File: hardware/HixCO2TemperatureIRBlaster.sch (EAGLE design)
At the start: 33 parts, among them J1 FTDI, J2 IEC320C8, J3 XH4P, Q1 AO3400, Q2 AO3400, U1 ESP12E, U2 LM3940, U3 HLK-PM01, U4 DS18B20

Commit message: update hardware
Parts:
- removed C3: 100nF, resistor:C-EUC1206
- removed R1, R3, R4: 10K, rcl:R-EU_R1206
- removed R13: 2.2K, rcl:R-EU_R1206
- removed S1: PROG, 0_HixField:PUSHBTN
- removed S2: RST, 0_HixField:PUSHBTN
- removed U1: ESP12E, 0_HixField:ESP8266(ESP12E)SMD
- added C5: 100nF, resistor:C-EUC1206
- added R10, R11, R15: 10K, rcl:R-EU_R1206
- added R12: 2.2K, rcl:R-EU_R1206
- added S3: RST, 0_HixField:PUSHBTNSMALL
- added S4: PROG, 0_HixField:PUSHBTNSMALL
- added U$1: MHZ-19_CO2, 0_HixField:MHZ-19_CO2
- added U$2: ESP8266(ESP12E)V2, 0_HixField:ESP8266(ESP12E)V2
- C1, C2: device resistor:C-EUC1206 -> rcl:CPOL-EUSMCA
- C6: device resistor:CPOL-EUE3.5-8 -> 0_HixField:ELCO
- IRLED1, IRLED2, IRLED3: value (none) -> LEDLED5MM_ANGLED1; device led:LED5MM -> 0_HixField:LEDLED5MM_ANGLED1
- R8, R9: device resistor:R-EU_R1206 -> rcl:R-EU_R1206
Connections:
- removed net ENABLE: R3.1, U1.ENABLE
- removed net GPIO0: R2.1, S1.1, U1.GPIO0
- removed net GPIO15: R4.2, U1.GPIO15
- removed net RESET: R1.1, S2.1, U1.RESET
- new net N$10: R2.2, U$2.CS_TXD2_GPIO15
- new net N$11: U$2.GPIO16_WAKE
- new net N$7: R10.1, S3.1, U$2.RST
- new net N$8: R11.1, U$2.ENABLE
- new net N$9: R15.1, S4.1, U$2.FLASH_GPIO0
- net 3.3V: now also C2.+, C5.1, J3.2, R10.2, R11.2, R12.2, R15.2, U$2.VCC; no longer C2.1, C3.1, R1.2, R13.2, R2.2, R3.2, U1.VCC
- net 5.0V: now also C1.+; no longer C1.1, J3.2
- net BEEP: now also R12.1, U$2.TXD1_GPIO2; no longer R13.1, U1.GPIO2
- net GND: now also C1.-, C2.-, C5.2, R2.1, S3.2, S4.2, U$2.GND; no longer C1.2, C2.2, C3.2, R4.1, S1.2, S2.2, U1.GND
- net IR_IN: now also U$2.GPIO14_SCLK; no longer U1.GPIO14
- net IR_OUT: now also U$2.GPIO13_MOSI; no longer U1.GPIO13
- net RXD: now also U$2.TXD0_GPIO1; no longer U1.TX
- net SCL: now also U$2.SCL_GPIO5; no longer U1.GPIO5
- net SDA: now also U$2.SDA_GPIO4; no longer U1.GPIO4
- net TEMP: now also U$2.GPIO12_MISO; no longer U1.GPIO12
- net TXD: now also U$2.RXD0_GPIO3; no longer U1.RX

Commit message: continued working on hardware models
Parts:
- C4: device resistor:C-EUC1206 -> rcl:C-EUC1206
- C5: device resistor:C-EUC1206 -> rcl:C-EUC1206; SPICEPREFIX (none) -> C
- C6: device 0_HixField:ELCO -> 0_HixField:ELCOELKO_RADIAL_STRAIGHT_4P_8D_9H
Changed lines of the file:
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@@
 <part name="F1" library="0_HixField" deviceset="FUSE" device="" value="800mA"/>
 <part name="R14" library="0_HixField" library_urn="urn:adsk.eagle:library:13392178" deviceset="S10K275" device="" package3d_urn="urn:adsk.eagle:package:12836052/2" value="S10K275"/>
-<part name="C6" library="0_HixField" library_urn="urn:adsk.eagle:library:13392178" deviceset="ELCO" device="" package3d_urn="urn:adsk.eagle:package:13392182/1" value="680μF/6.3V"/>
+<part name="C6" library="0_HixField" library_urn="urn:adsk.eagle:library:13392178" deviceset="ELCO" device="ELKO_RADIAL_STRAIGHT_4P_8D_9H" package3d_urn="urn:adsk.eagle:package:17790431/3" value="680μF/6.3V"/>
 <part name="SUPPLY1" library="0_HixField" library_urn="urn:adsk.eagle:library:13392178" deviceset="5.0V" device=""/>
 <part name="SUPPLY2" library="0_HixField" library_urn="urn:adsk.eagle:library:13392178" deviceset="3.3V" device=""/>
 <part name="J2" library="0_HixField" library_urn="urn:adsk.eagle:library:13392178" deviceset="IEC320C8" device="" package3d_urn="urn:adsk.eagle:package:17723124/3"/>
-<part name="J1" library="0_HixField" deviceset="FTDI" device=""/>
+<part name="J1" library="0_HixField" library_urn="urn:adsk.eagle:library:13392178" deviceset="FTDI" device="" package3d_urn="urn:adsk.eagle:package:12836035/3"/>
 <part name="GND3" library="supply1" deviceset="GND" device=""/>
-<part name="B1" library="0_HixField" deviceset="BUZZER(12MM)" device=""/>
+<part name="B1" library="0_HixField" library_urn="urn:adsk.eagle:library:13392178" deviceset="BUZZER(12MM)" device="" package3d_urn="urn:adsk.eagle:package:12836039/1"/>
 <part name="GND10" library="supply1" deviceset="GND" device=""/>
 <part name="R9" library="rcl" library_urn="urn:adsk.eagle:library:334" deviceset="R-EU_" device="R1206" package3d_urn="urn:adsk.eagle:package:23540/2" value="4.7K"/>
@@
 <part name="R8" library="rcl" library_urn="urn:adsk.eagle:library:334" deviceset="R-EU_" device="R1206" package3d_urn="urn:adsk.eagle:package:23540/2" value="100"/>
 <part name="GND9" library="supply1" deviceset="GND" device=""/>
-<part name="C4" library="resistor" deviceset="C-EU" device="C1206" value="4.7μF"/>
+<part name="C4" library="rcl" library_urn="urn:adsk.eagle:library:334" deviceset="C-EU" device="C1206" package3d_urn="urn:adsk.eagle:package:23618/2" value="4.7μF"/>
 <part name="SUPPLY13" library="0_HixField" library_urn="urn:adsk.eagle:library:13392178" deviceset="3.3V" device=""/>
 <part name="U$1" library="0_HixField" library_urn="urn:adsk.eagle:library:13392178" deviceset="MHZ-19_CO2" device="" package3d_urn="urn:adsk.eagle:package:17734911/3"/>
@@
 <part name="GND11" library="supply1" deviceset="GND" device=""/>
 <part name="SUPPLY14" library="0_HixField" library_urn="urn:adsk.eagle:library:13392178" deviceset="3.3V" device=""/>
-<part name="C5" library="resistor" deviceset="C-EU" device="C1206" value="100nF"/>
+<part name="C5" library="rcl" library_urn="urn:adsk.eagle:library:334" deviceset="C-EU" device="C1206" package3d_urn="urn:adsk.eagle:package:23618/2" value="100nF">
+<spice>
+<pinmapping spiceprefix="C">
+<pinmap gate="G$1" pin="1" pinorder="1"/>
+<pinmap gate="G$1" pin="2" pinorder="2"/>
+</pinmapping>
+</spice>
+<attribute name="SPICEPREFIX" value="C"/>
+</part>
 <part name="GND12" library="supply1" deviceset="GND" device=""/>
 <part name="S3" library="0_HixField" library_urn="urn:adsk.eagle:library:13392178" deviceset="PUSHBTN" device="SMALL" package3d_urn="urn:adsk.eagle:package:12836051/3" value="RST"/>
@@
 </nets>
 </sheet>
-<sheet>
-<plain>
-</plain>
-<instances>
-</instances>
-<busses>
-</busses>
-<nets>
-</nets>
-</sheet>

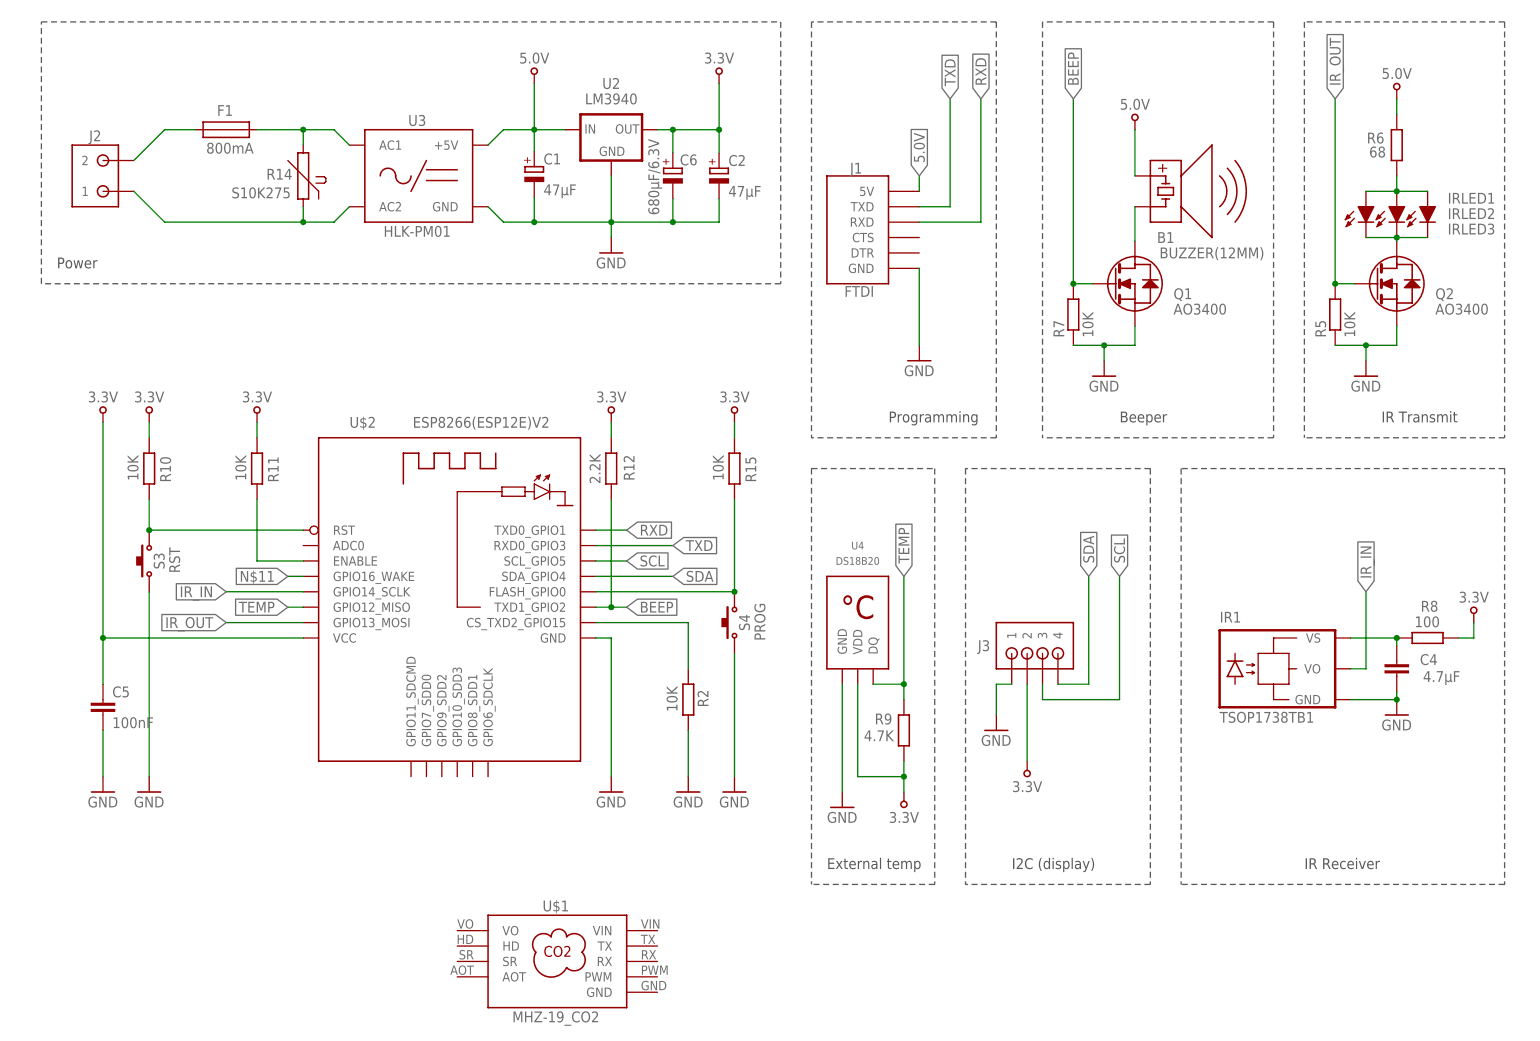
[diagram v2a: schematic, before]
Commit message: updated esp pin mapping
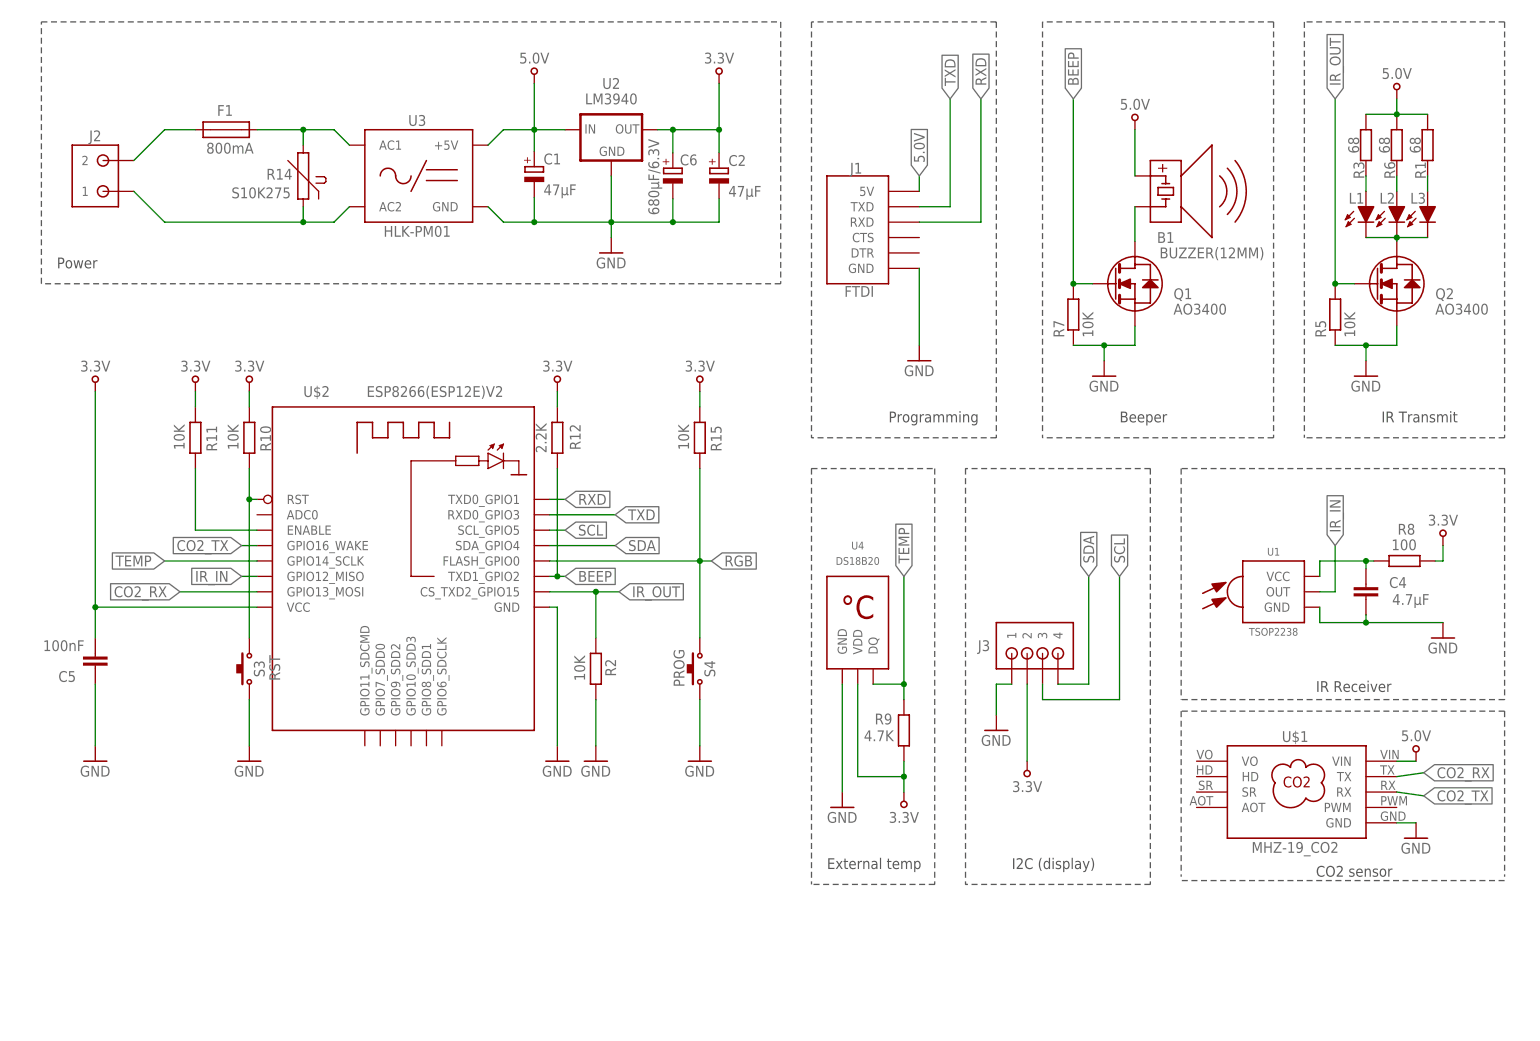
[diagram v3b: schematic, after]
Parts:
- removed IR1: TSOP1738TB1, telefunken:TSOP1738TB1
- added R1, R3: 68, rcl:R-EU_0204/7
- added U1: TSOP2238, 0_HixField:TSOP2238
- R6: device rcl:R-EU_R1206 -> rcl:R-EU_0204/7
- renumbered IRLED1 to L1, IRLED2 to L2, IRLED3 to L3
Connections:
- net N$9 renamed RGB
- removed net N$11: U$2.GPIO16_WAKE
- new net CO2_RX: U$1.TX, U$2.GPIO13_MOSI
- new net CO2_TX: U$1.RX, U$2.GPIO16_WAKE
- new net N$9: L1.A, R3.1
- net 5.0V: now also R1.2, R3.2, U$1.VIN
- net GND: now also U$1.GND, U1.GND; no longer IR1.GND
- net IR_IN: now also U$2.GPIO12_MISO, U1.OUT; no longer IR1.VO, U$2.GPIO14_SCLK
- net IR_OUT: now also R2.2, U$2.CS_TXD2_GPIO15; no longer U$2.GPIO13_MOSI
- net N$10: now also L3.A, R1.1; no longer R2.2, U$2.CS_TXD2_GPIO15
- net N$4: no longer L1.A, L3.A
- net N$6: now also U1.VCC; no longer IR1.VS
- net TEMP: now also U$2.GPIO14_SCLK; no longer U$2.GPIO12_MISO
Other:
- note added: "CO2 sensor"
- moved on the sheet: C4, C5, R10, R11, R12, R15, R2, R8, S3, S4, U$1, U$2

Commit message: electronic hardware v1 complete
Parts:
- added C3: 100nF, rcl:C-EUC1206
- added U$3: LED_RGB, 0_HixField:LED_RGB
- F1: value 800mA -> 800mA 250V
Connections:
- net 5.0V: now also C3.1, U$3.VCC
- net GND: now also C3.2, U$3.GND
- net RGB: now also U$3.DIN
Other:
- note added: "RGB LED"
- moved on the sheet: B1, C4, C5, J1, J3, L1, L2, L3, Q1, Q2, R1, R10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
